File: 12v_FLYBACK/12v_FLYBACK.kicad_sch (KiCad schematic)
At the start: 11 parts, among them J1 AC Input, T1 Transformer_1P_2S

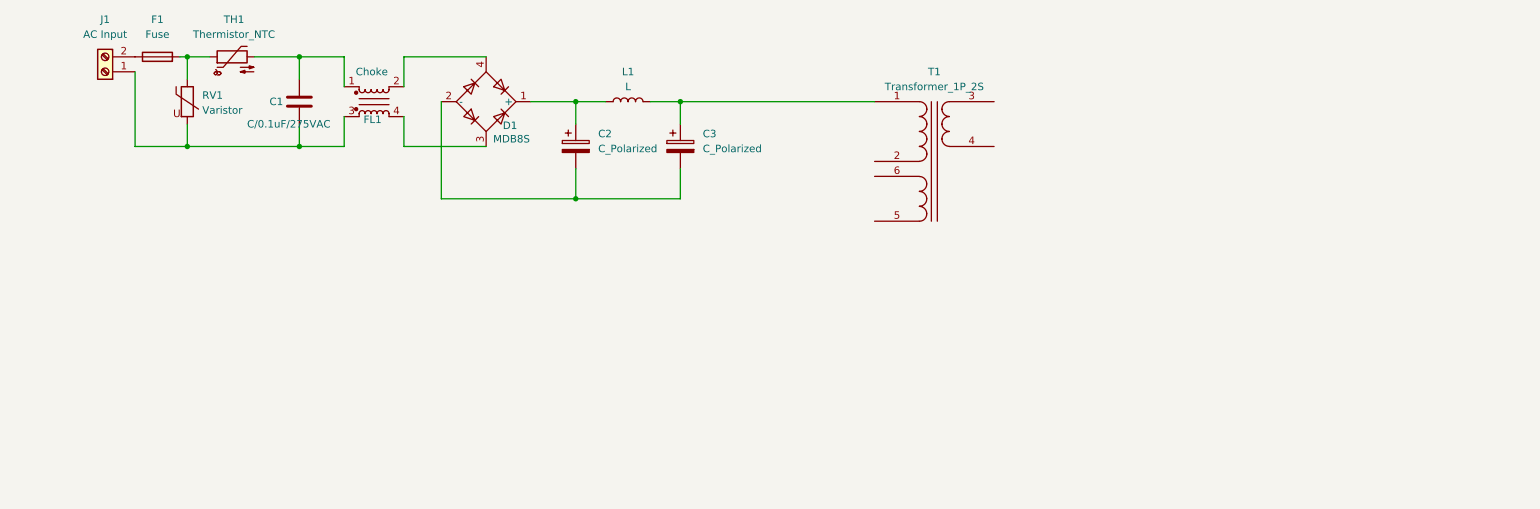
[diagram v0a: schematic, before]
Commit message: Schematic done
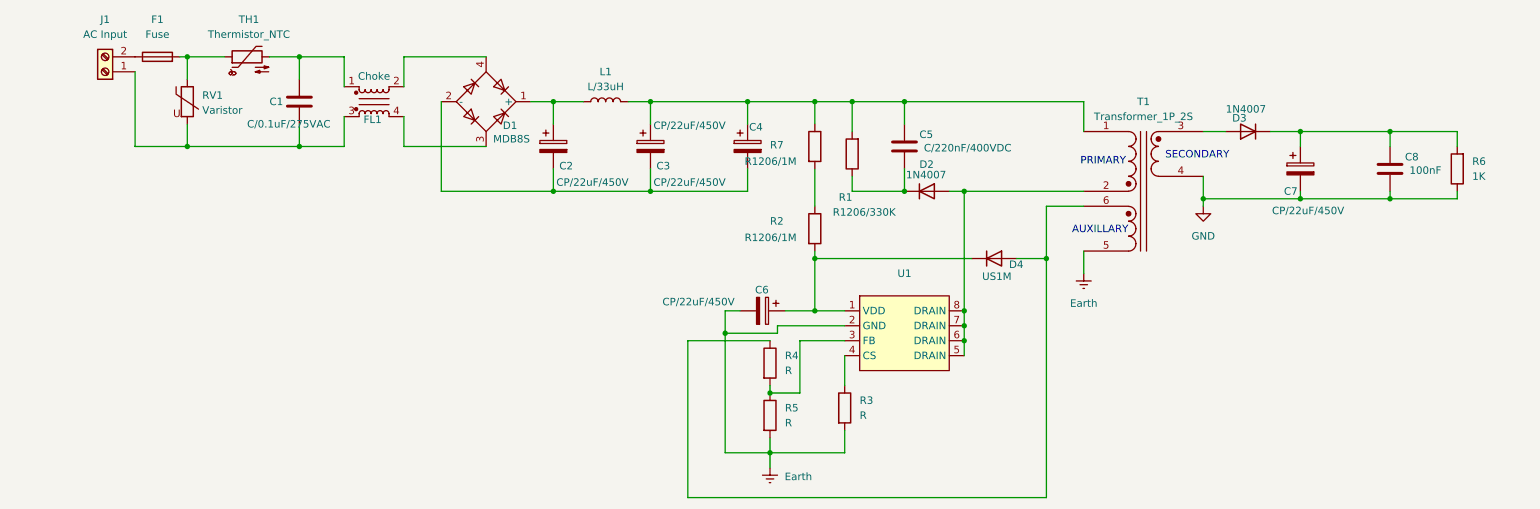
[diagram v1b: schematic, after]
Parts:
- added C4: CP/22uF/450V, Capacitor_THT:CP_Radial_D12.5mm_P5.00mm, symbol Device:C_Polarized
- added C5: C/220nF/400VDC, Capacitor_THT:C_Rect_L18.0mm_W6.0mm_P15.00mm_FKS3_FKP3, symbol Device:C
- added C6, C7: CP/22uF/450V, symbol Device:C_Polarized
- added C8: 100nF, Capacitor_SMD:C_0603_1608Metric, symbol Device:C
- added D2, D3: 1N4007, Diode_THT:D_DO-41_SOD81_P10.16mm_Horizontal, symbol Diode:1N4007
- added D4: US1M, Diode_THT:D_DO-41_SOD81_P10.16mm_Horizontal, symbol Diode:1N4007
- added R1: R1206/330K, symbol Device:R
- added R2, R7: R1206/1M, symbol Device:R
- added R3, R4, R5: R, symbol Device:R
- added R6: 1K, symbol Device:R
- added U1: ~, Package_DIP:DIP-8_W7.62mm, symbol HARDWARE_DFM:KP21827
- C1: footprint (none) -> Capacitor_THT:C_Rect_L16.5mm_W6.0mm_P15.00mm_MKT
- C2, C3: value C_Polarized -> CP/22uF/450V; footprint (none) -> Capacitor_THT:CP_Radial_D12.5mm_P5.00mm
- F1: footprint (none) -> MinhDfm:FUSE_T2A250V
- FL1: footprint Inductor_THT:Choke_Schaffner_RN102-04-14.0x14.0mm -> (none)
- L1: value L -> L/33uH
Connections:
- net at C2.2, C3.2, D1.2 (-): now also C4.2
- net at C3.1, L1.2, T1.1 (AA): now also C4.1, C5.1, R1.2, R7.1
- net at T1.2 (AB): now also D2.2 (A), U1.5 (DRAIN), U1.6 (DRAIN), U1.7 (DRAIN), U1.8 (DRAIN)
- net at T1.3 (SA): now also D3.2 (A)
- net GND: now reaches T1.4 (SB)
- net GND: now also C7.2, C8.2, R6.1
- net Earth: now reaches T1.5 (SC)
- net Earth: now also C6.2, R3.2, R5.2, U1.2 (GND)
- net at T1.6 (SD): now also D4.2 (A), R4.1
- new net: C5.2, D2.1 (K), R1.1
- new net: C7.1, C8.1, D3.1 (K), R6.2
- new net: R2.1, R7.2
- new net: C6.1, D4.1 (K), R2.2, U1.1 (VDD)
- new net: R4.2, R5.1, U1.3 (FB)
- new net: R3.1, U1.4 (CS)
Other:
- note added: "AUXILLARY"
- note added: "PRIMARY"
- note added: "SECONDARY"
- moved on the sheet: C2, L1, TH1

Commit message: New update
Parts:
- C6: value CP/22uF/450V -> CP/5uF/50V
- C8: value 100nF -> C0603/100nF
- F1: value Fuse -> T2A250V
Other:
- moved on the sheet: C1, F1, J1, R6, R7, RV1, TH1
